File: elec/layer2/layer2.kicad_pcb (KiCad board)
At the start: 2 copper layers, 1 part

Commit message: feat: did something
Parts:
- added H1: MountingHole, MountingHole:MountingHole_3.2mm_M3_DIN965_Pad, F.Cu at (80.9, 33.9)
- added H10: MountingHole, MountingHole:MountingHole_3.2mm_M3_DIN965_Pad, F.Cu at (191.1, 144.1)
- added H11: MountingHole, MountingHole:MountingHole_3.2mm_M3_DIN965_Pad, F.Cu at (82.9, 185.4)
- added H12: MountingHole, MountingHole:MountingHole_3.2mm_M3_DIN965_Pad, F.Cu at (148.7, 185.4)
- added H2: MountingHole, MountingHole:MountingHole_3.2mm_M3_DIN965_Pad, F.Cu at (150.7, 33.9)
- added H3: MountingHole, MountingHole:MountingHole_3.2mm_M3_DIN965_Pad, F.Cu at (40.5, 74.4)
- added H4: MountingHole, MountingHole:MountingHole_3.2mm_M3_DIN965_Pad, F.Cu at (191.1, 74.4)
- added H5: MountingHole, MountingHole:MountingHole_3.2mm_M3_DIN965_Pad, F.Cu at (75.8, 86.7)
- added H6: MountingHole, MountingHole:MountingHole_3.2mm_M3_DIN965_Pad, F.Cu at (155.8, 86.7)
- added H7: MountingHole, MountingHole:MountingHole_3.2mm_M3_DIN965_Pad, F.Cu at (75.8, 131.7)
- added H8: MountingHole, MountingHole:MountingHole_3.2mm_M3_DIN965_Pad, F.Cu at (155.8, 131.7)
- added H9: MountingHole, MountingHole:MountingHole_3.2mm_M3_DIN965_Pad, F.Cu at (40.5, 144.1)
- added U2: ~, layer2-pcb-footprints:motor-driver-module, B.Cu at (47.8, 109.2)
- added U3: ~, layer2-pcb-footprints:motor-driver-module, B.Cu at (183.8, 109.2)
- added U4: ~, layer2-pcb-footprints:motor-driver-module, F.Cu at (100.3, 67.2)
- added U5: ~, layer2-pcb-footprints:motor-driver-module, F.Cu at (131.3, 67.2)
- U1: moved to B.Cu
- moved U1 67.1 mm to (115.8, 39.2), turned to 90 degrees
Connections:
- U1 pad 2: unconnected-(U1-GND-Pad2) -> GND
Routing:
- added copper zone on B.Cu, net GND
- added copper zone on F.Cu, net GND
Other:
- board outline added: 178 x 173.3 mm

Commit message: did smth
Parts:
- added BatteryConnection1: Conn_01x02, layer2-pcb-footprints:AMASS_XT60-M, F.Cu at (190.5, 42.1)
- added KillSwitch1: Conn_01x02, layer2-pcb-footprints:AMASS_XT60-M, F.Cu at (190.5, 51.7)

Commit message: did some stuff on l2
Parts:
- removed U5: ~, layer2-pcb-footprints:motor-driver-module
- added DribblerConnection1: Conn_01x03, Pinheaders:PinHeader_1x03_P2.54mm_Vertical, F.Cu at (218.3, 40.2)
- added DribblerConnection2: Conn_01x02, Connector_AMASS:AMASS_XT30U-F_1x02_P5.0mm_Vertical, F.Cu at (215.8, 32.2)
- added L1-->L2Connection1: Conn_01x08, Pinheaders:PinHeader_1x08_P2.54mm_Vertical, F.Cu at (252.8, 13.6)
- added L1-->L2Connection2: Conn_01x08, Pinheaders:PinHeader_1x08_P2.54mm_Vertical, F.Cu at (266.2, 13.6)
- added L2-->L3Connection1: Conn_01x08, Pinheaders:PinHeader_1x08_P2.54mm_Vertical, F.Cu at (205.2, 30.9)
- added L2-->L3Connection2: Conn_01x08, Pinheaders:PinHeader_1x08_P2.54mm_Vertical, F.Cu at (209.9, 30.9)
- added Lightgate(LDR)1: Conn_01x02, Connector_JST:JST_SH_BM02B-SRSS-TB_1x02-1MP_P1.00mm_Vertical, F.Cu at (166.5, 49.4)
- added Lightgate(LED)1: Conn_01x02, Connector_JST:JST_SH_BM02B-SRSS-TB_1x02-1MP_P1.00mm_Vertical, F.Cu at (166.5, 55.7)
- BatteryConnection1, KillSwitch1: footprint layer2-pcb-footprints:AMASS_XT60-M -> Connector_AMASS:AMASS_XT30U-F_1x02_P5.0mm_Vertical
- U4: value ~ -> DEV-15583; footprint layer2-pcb-footprints:motor-driver-module -> layer2-pcb-footprints:MODULE_DEV-15583
- moved BatteryConnection1 69.8 mm to (195.1, 111.7), turned to 90 degrees
- moved U4 15.2 mm to (115.0, 63.6), turned to 90 degrees
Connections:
- U1 pad 1: unconnected-(U1-12v-Pad1) -> +12V
- U1 pad 3: unconnected-(U1-3v3-Pad3) -> +3V3
- U1 pad 4: unconnected-(U1-5v-Pad4) -> +5V
- U2 pad 1: unconnected-(U2-12v-Pad1) -> +12V
- U2 pad 2: unconnected-(U2-3v3-Pad2) -> +3V3
- U2 pad 3: unconnected-(U2-EN-Pad3) -> /M SW
- U2 pad 4: unconnected-(U2-MOTOR_IN_A-Pad4) -> /M3 IN A
- U2 pad 5: unconnected-(U2-MOTOR_IN_B-Pad5) -> /M3 IN B
- U2 pad 6: unconnected-(U2-MOTOR_PWM-Pad6) -> /M3 PWM
- U3 pad 1: unconnected-(U3-12v-Pad1) -> +12V
- U3 pad 2: unconnected-(U3-3v3-Pad2) -> +3V3
- U3 pad 3: unconnected-(U3-EN-Pad3) -> /M SW
- U3 pad 4: unconnected-(U3-MOTOR_IN_A-Pad4) -> /M4 IN A
- U3 pad 5: unconnected-(U3-MOTOR_IN_B-Pad5) -> /M4 IN B
- U3 pad 6: unconnected-(U3-MOTOR_PWM-Pad6) -> /M4 PWM
- U4 pad 7: GND -> unconnected-(U4-Pad7)
- U4 pad 8: (no net) -> unconnected-(U4-Pad8)

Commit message: did something
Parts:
- added KillSwitch2: SW_SPST, Connector_AMASS:AMASS_XT30U-F_1x02_P5.0mm_Vertical, F.Cu at (217.1, 61.0)
- moved L1-->L2Connection2 181.4 mm to (94.1, 70.9), turned to 180 degrees
- moved Lightgate(LDR)1 135.6 mm to (85.6, 158.2), turned to 90 degrees
- moved L1-->L2Connection1 126.2 mm to (140.3, 70.8), turned to 180 degrees
- moved L2-->L3Connection1 121.9 mm to (90.1, 70.9), turned to 180 degrees
- moved Lightgate(LED)1 104.6 mm to (146.1, 158.2), turned to -90 degrees
- moved L2-->L3Connection2 83.9 mm to (136.1, 70.9), turned to 180 degrees
- moved KillSwitch1 62.8 mm to (180.3, 113.7)
- moved DribblerConnection2 49.5 mm to (261.3, 51.7)
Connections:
- BatteryConnection1 pad 1: Net-(BatteryConnection1-Pin_1) -> GND
- BatteryConnection1 pad 2: +12V -> Net-(BatteryConnection1-Pin_2)
- KillSwitch1 pad 2: Net-(BatteryConnection1-Pin_1) -> Net-(KillSwitch1-Pin_2)
- L1-->L2Connection2 pad 4: /RX -> /TX
- L1-->L2Connection2 pad 5: /TX -> /RX
- U4 pad 0: unconnected-(U4-Pad0) -> /RX
- U4 pad 1: unconnected-(U4-Pad1) -> /TX
- U4 pad 16: /LightGateLDR -> unconnected-(U4-Pad16)
- U4 pad 17: /Dribbler Data -> unconnected-(U4-Pad17)
- U4 pad 18: /M4 IN A -> unconnected-(U4-Pad18)
- U4 pad 19: /M4 IN B -> unconnected-(U4-Pad19)
- U4 pad 2: unconnected-(U4-Pad2) -> /LightGateLDR
- U4 pad 20: /M4 PWM -> unconnected-(U4-Pad20)
- U4 pad 21: /M3 IN A -> unconnected-(U4-Pad21)
- U4 pad 22: /M3 IN B -> unconnected-(U4-Pad22)
- U4 pad 23: /M3 PWM -> unconnected-(U4-Pad23)
- U4 pad 3: unconnected-(U4-Pad3) -> /Dribbler Data
- U4 pad 4: unconnected-(U4-Pad4) -> /M3 IN A
- U4 pad 5: unconnected-(U4-Pad5) -> /M3 IN B
- U4 pad 6: unconnected-(U4-Pad6) -> /M3 PWM
- U4 pad 7: unconnected-(U4-Pad7) -> /M4 IN A
- U4 pad 8: unconnected-(U4-Pad8) -> /M4 IN B
- U4 pad 9: unconnected-(U4-Pad9) -> /M4 PWM

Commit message: did smnth to l2
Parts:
- removed L2-->L3Connection1, L2-->L3Connection2: Conn_01x08, Pinheaders:PinHeader_1x08_P2.54mm_Vertical
- moved L1-->L2Connection1 44.0 mm to (96.3, 71.2)
- moved L1-->L2Connection2 43.0 mm to (137.1, 70.9)
- moved DribblerConnection2 6.18 mm to (255.3, 53.2)
- moved U4 3.50 mm to (117.1, 60.7)
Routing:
- net +3V3: track 0.00 -> 10.2 mm
- net +5V: track 0.00 -> 10.1 mm
- net +12V: track 0.00 -> 5.08 mm

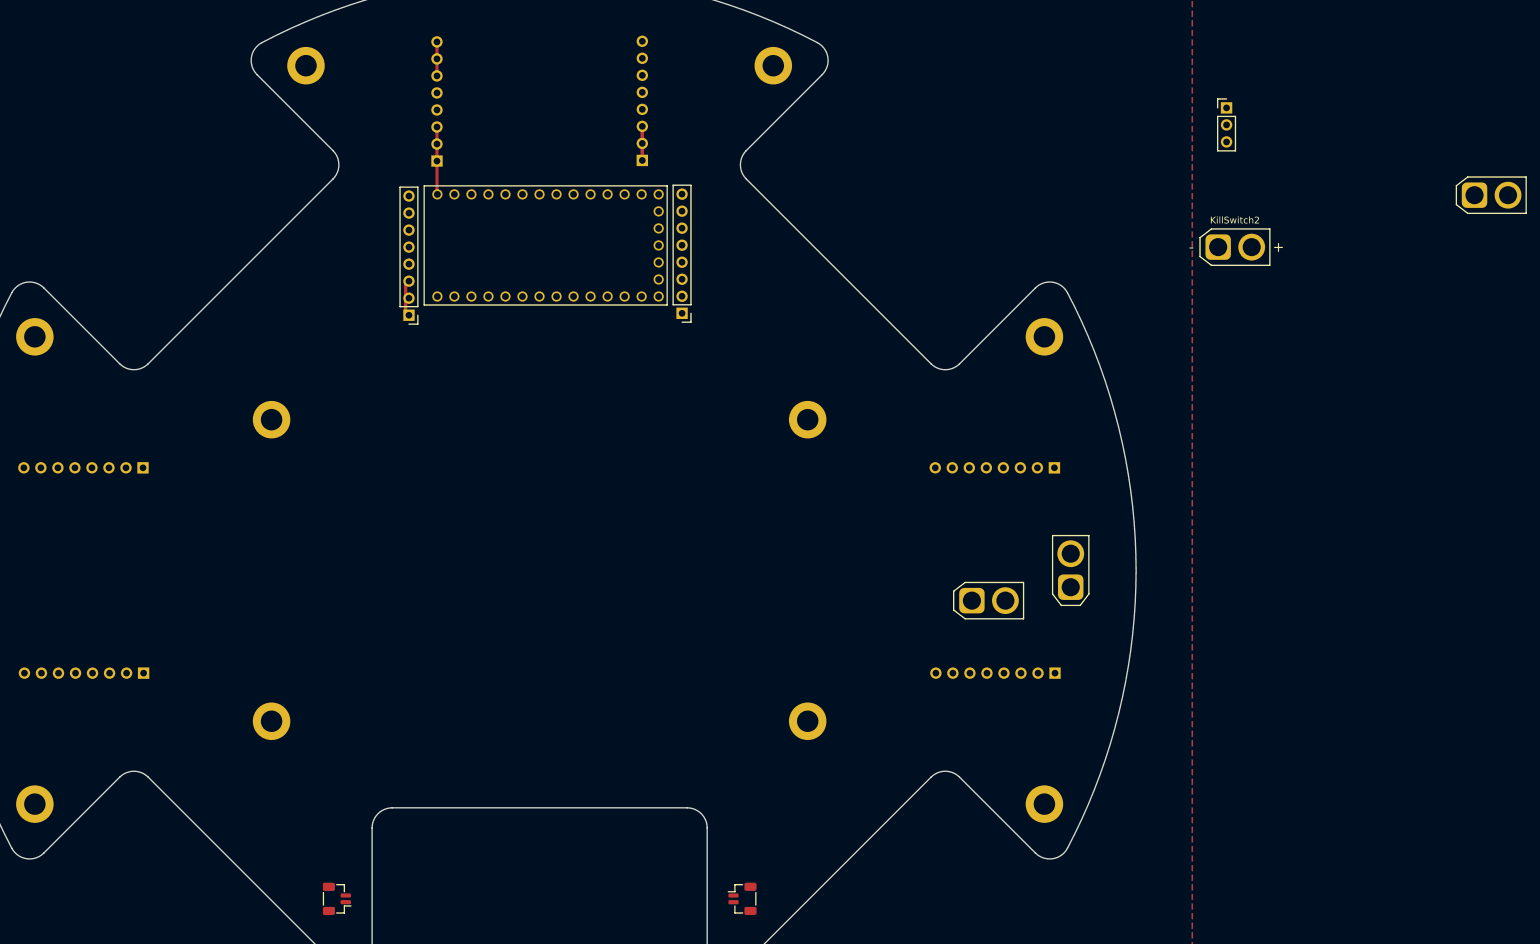
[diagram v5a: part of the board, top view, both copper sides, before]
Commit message: FInished L2-l3 connection and branding
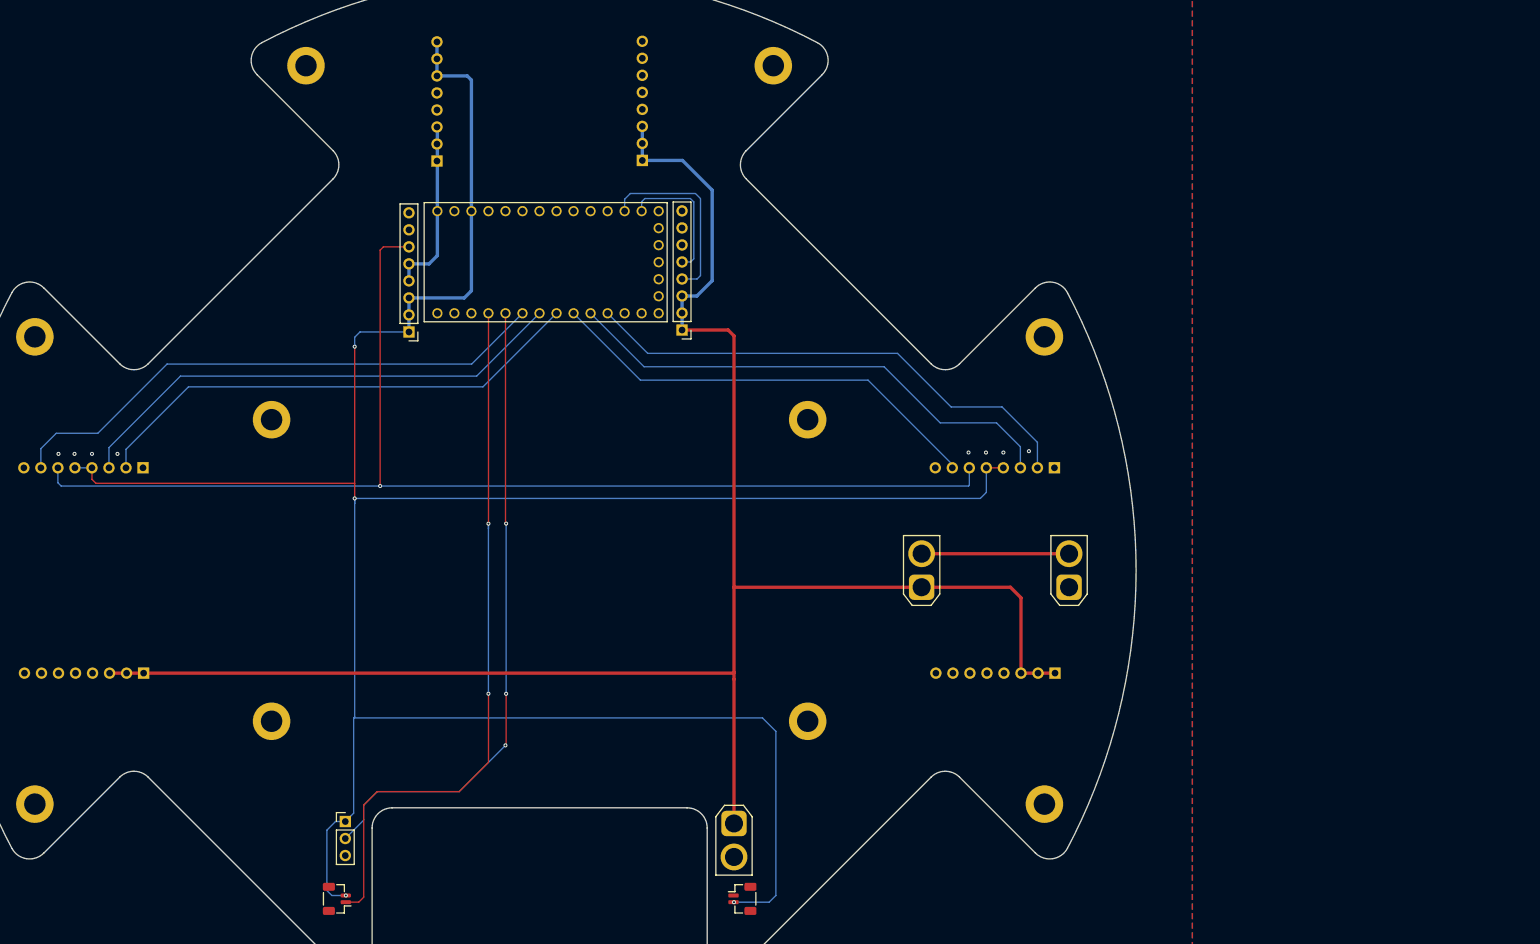
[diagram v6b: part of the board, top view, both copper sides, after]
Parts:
- removed KillSwitch1: Conn_01x02, Connector_AMASS:AMASS_XT30U-F_1x02_P5.0mm_Vertical
- moved DribblerConnection1 169.2 mm to (86.8, 146.7)
- moved DribblerConnection2 144.9 mm to (144.8, 147.0), turned to -90 degrees
- moved KillSwitch2 67.3 mm to (172.8, 111.7), turned to 90 degrees
- moved L1-->L2Connection1 2.50 mm to (96.3, 73.7)
- moved L1-->L2Connection2 2.50 mm to (137.1, 73.4)
- moved U4 2.50 mm to (117.1, 63.2)
- moved BatteryConnection1 0.25 mm to (194.8, 111.7)
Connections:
- U4 pad 0: /RX -> unconnected-(U4-Pad0)
- U4 pad 1: /TX -> unconnected-(U4-Pad1)
- U4 pad 14: unconnected-(U4-Pad14) -> /RX
- U4 pad 15: unconnected-(U4-Pad15) -> /TX
- U4 pad 3.3V_1: +3V3 -> unconnected-(U4-Pad3.3V_1)
- U4 pad 5: /M3 IN B -> /M3 PWM
- U4 pad 6: /M3 PWM -> /M3 IN B
- U4 pad 8: /M4 IN B -> /M4 PWM
- U4 pad 9: /M4 PWM -> /M4 IN B
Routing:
- net +3V3: track 10.2 -> 394.1 mm, vias 0 -> 4
- net +12V: track 5.08 -> 275.2 mm
- net /M SW: track 0.00 -> 180.8 mm, vias 0 -> 1
- net /LightGateLDR: track 0.00 -> 105.4 mm, vias 0 -> 2
- net /Dribbler Data: track 0.00 -> 95.6 mm, vias 0 -> 3
- net /M3 IN A: track 0.00 -> 83.1 mm
- net /M4 IN B: track 0.00 -> 75.9 mm
- net /M3 PWM: track 0.00 -> 75.6 mm
- net /M4 PWM: track 0.00 -> 75.5 mm
- net /M3 IN B: track 0.00 -> 75.4 mm
- net /M4 IN A: track 0.00 -> 66.4 mm
- net /TX: track 0.00 -> 28.5 mm
- net Net-(BatteryConnection1-Pin_2): track 0.00 -> 22.0 mm
- net /RX: track 0.00 -> 20.0 mm
- net +5V: track 10.1 -> 26.5 mm
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
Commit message: stuff
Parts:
- added J1: Conn_01x08, Pinheaders:PinHeader_1x08_P2.54mm_Vertical, F.Cu at (258.6, 95.8)
- added J2: Conn_01x08, Pinheaders:PinHeader_1x08_P2.54mm_Vertical, F.Cu at (258.5, 126.5)
- added J3: Conn_01x08, Connector_PinSocket_2.54mm:PinSocket_1x08_P2.54mm_Vertical, F.Cu at (216.0, 144.7)
- added J4: Conn_01x08, Connector_PinSocket_2.54mm:PinSocket_1x08_P2.54mm_Vertical, F.Cu at (246.7, 144.8)
- added L2-->L3Connection1: Conn_01x08, Pinheaders:PinHeader_1x08_P2.54mm_Vertical, F.Cu at (247.6, 95.5)
- added U3: ~, layer2-pcb-footprints:motor-driver-module, F.Cu at (267.4, 111.1)
- added U3: ~, layer2-pcb-footprints:motor-driver-module, F.Cu at (231.4, 135.9)

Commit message: l2 domne
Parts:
- removed L1-->L2Connection1, L1-->L2Connection2, L2-->L3Connection1: Conn_01x08, Pinheaders:PinHeader_1x08_P2.54mm_Vertical
- removed U4: DEV-15583, layer2-pcb-footprints:MODULE_DEV-15583
- added Driver1: Conn_01x08, Connector_JST:JST_XH_B8B-XH-AM_1x08_P2.50mm_Vertical, F.Cu at (192.3, 85.6)
- added Driver2: Conn_01x08, Connector_JST:JST_XH_B8B-XH-AM_1x08_P2.50mm_Vertical, F.Cu at (56.7, 133.8)
- added Driver3: Conn_01x08, Connector_JST:JST_XH_B8B-XH-AM_1x08_P2.50mm_Vertical, F.Cu at (56.6, 85.9)
- added Driver4: Conn_01x08, Connector_JST:JST_XH_B8B-XH-AM_1x08_P2.50mm_Vertical, F.Cu at (192.7, 133.9)
- added L1-->l2Connection1: Conn_01x09, Pinheaders:PinHeader_1x09_P2.54mm_Vertical, F.Cu at (93.6, 47.3)
- added L2-->l2Connection2: Conn_01x09, Pinheaders:PinHeader_1x09_P2.54mm_Vertical, F.Cu at (138.0, 47.3)
- BatteryConnection1: footprint Connector_AMASS:AMASS_XT30U-F_1x02_P5.0mm_Vertical -> Connector_AMASS:AMASS_XT60-F_1x02_P7.20mm_Vertical
- moved J1 171.4 mm to (93.2, 50.9)
- moved J2 171.4 mm to (93.1, 81.6)
- moved U3 171.4 mm to (102.0, 66.2)
- moved J4 138.1 mm to (123.9, 81.5), turned to 90 degrees
- moved J3 131.4 mm to (124.0, 50.9), turned to 90 degrees
- moved U3 120.7 mm to (132.8, 66.2), turned to 0 degrees
- moved BatteryConnection1 2.58 mm to (196.3, 113.8)
- turned U1 to -90 degrees
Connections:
- U2 pad 3: /M SW -> /M SW3
- U3 pad 3: /M SW -> /M SW4
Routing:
- net /M SW: track 180.8 -> 75.0 mm, vias 1 -> 0
- net +12V: track 275.2 -> 364.4 mm
- net /Sol: track 0.00 -> 83.1 mm, vias 0 -> 2
- net /M3 IN A: track 83.1 -> 8.33 mm
- net /M3 IN B: track 75.4 -> 7.84 mm
- net /M3 PWM: track 75.6 -> 8.26 mm
- net /M4 IN B: track 75.9 -> 8.75 mm
- net /M4 PWM: track 75.5 -> 8.65 mm
- net /M4 IN A: track 66.4 -> 8.62 mm
- net +24V: track 0.00 -> 57.0 mm
- net /RX: track 20.0 -> 70.6 mm
- net /TX: track 28.5 -> 72.5 mm
- net +5V: track 26.5 -> 68.6 mm
- net Net-(BatteryConnection1-Pin_2): track 22.0 -> 0.00 mm
- net /LightGateLDR: track 105.4 -> 122.2 mm
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- added copper zone on F.Cu, net +12V
- added copper zone on F.Cu, net Net-(BatteryConnection1-Pin_2)
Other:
- board text added: "BUCK"
